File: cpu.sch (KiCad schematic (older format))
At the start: 26 parts, among them P27 BDM, U1 MC9S12XDP512, X1 16MHz

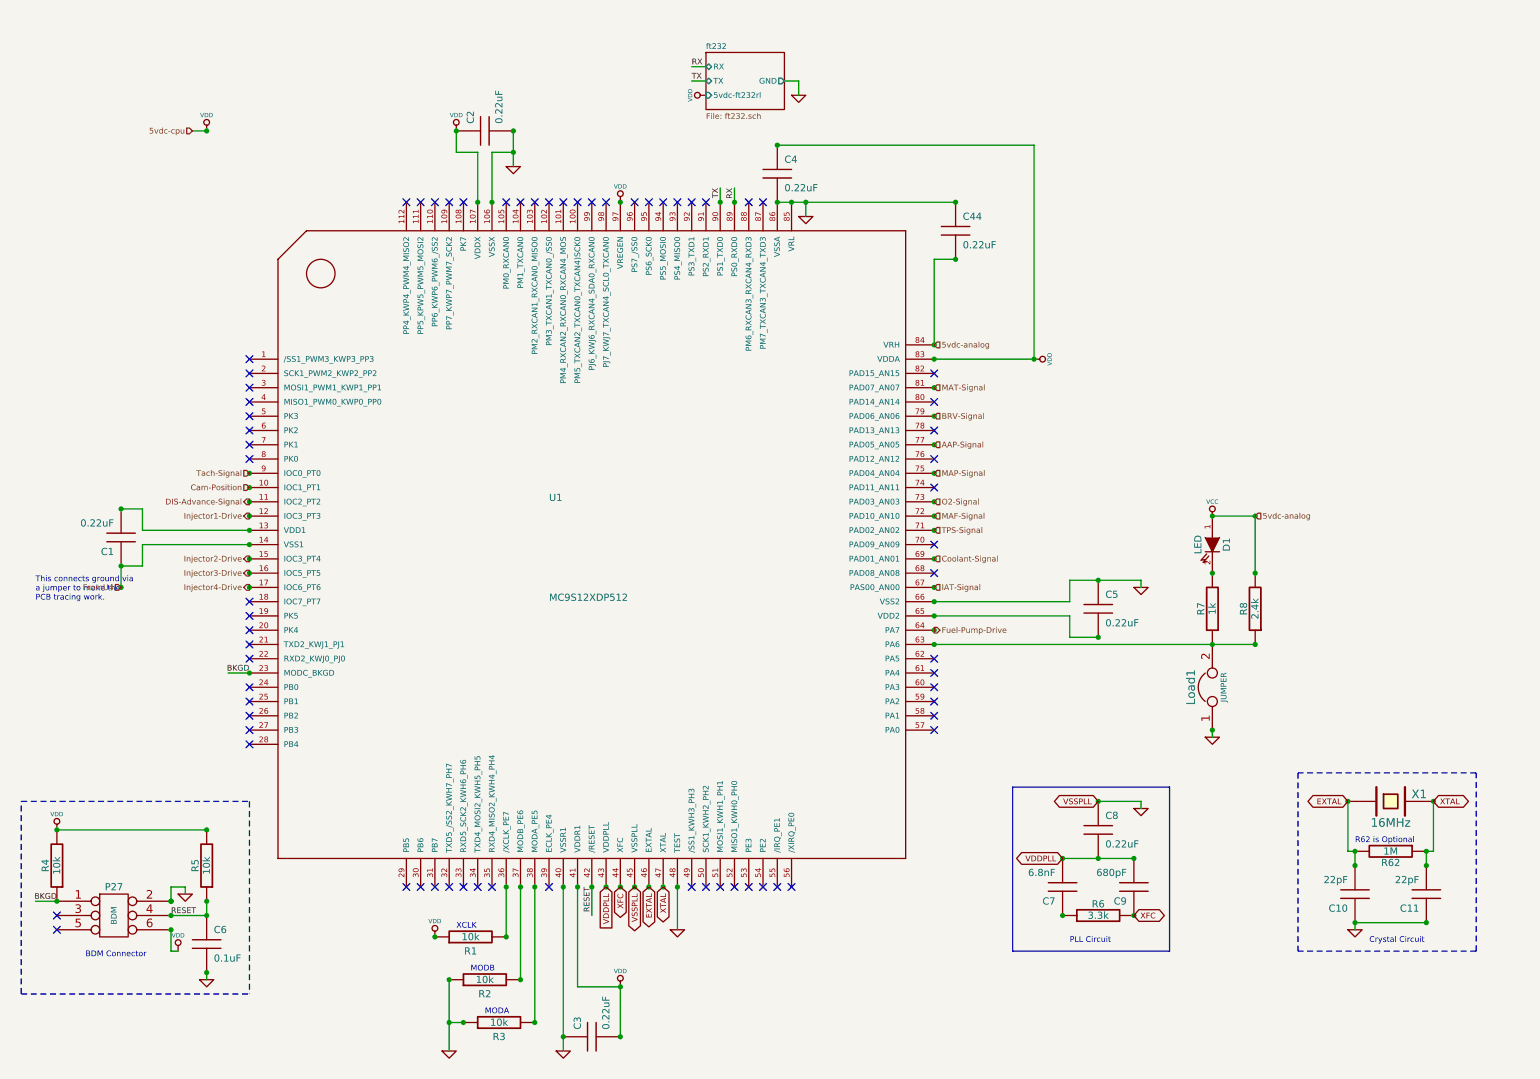
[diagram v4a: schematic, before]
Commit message: Fix MAX9926 Configuration and created new PCB and PDF
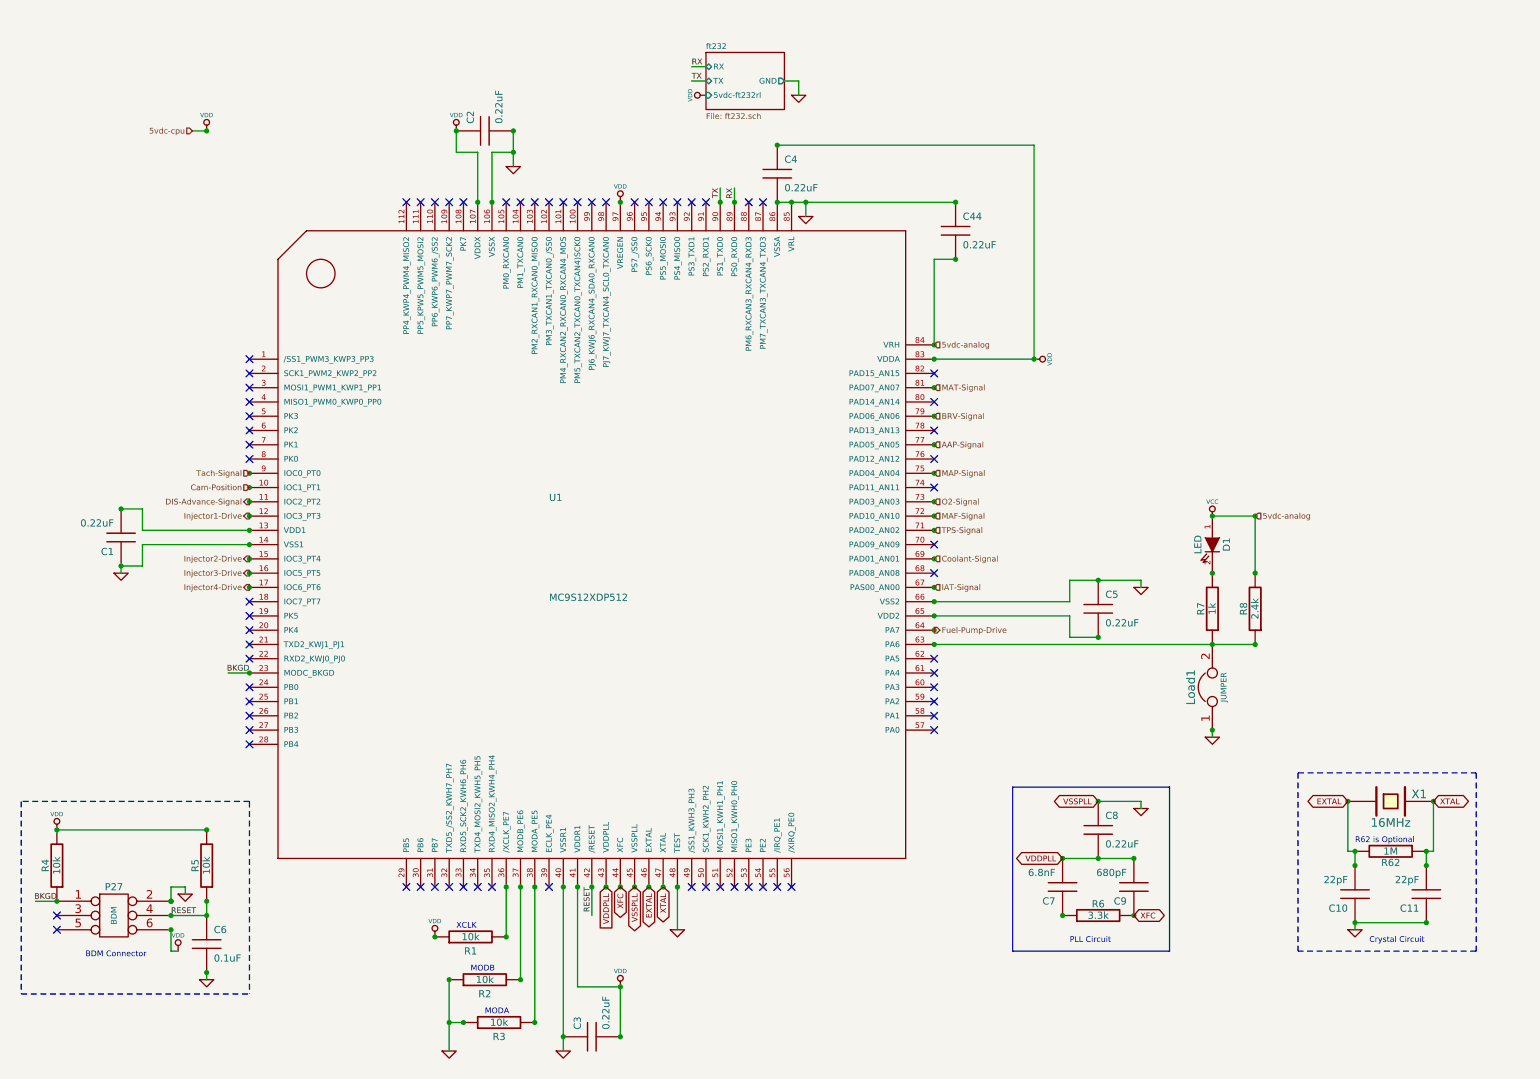
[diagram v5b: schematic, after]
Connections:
- net labels removed: FromU4
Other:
- note removed: "This connects ground via \na jumper to make the \nPCB tracing work."

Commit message: Updated Schematics and PDF, uploaded mc9s12xdp512 library
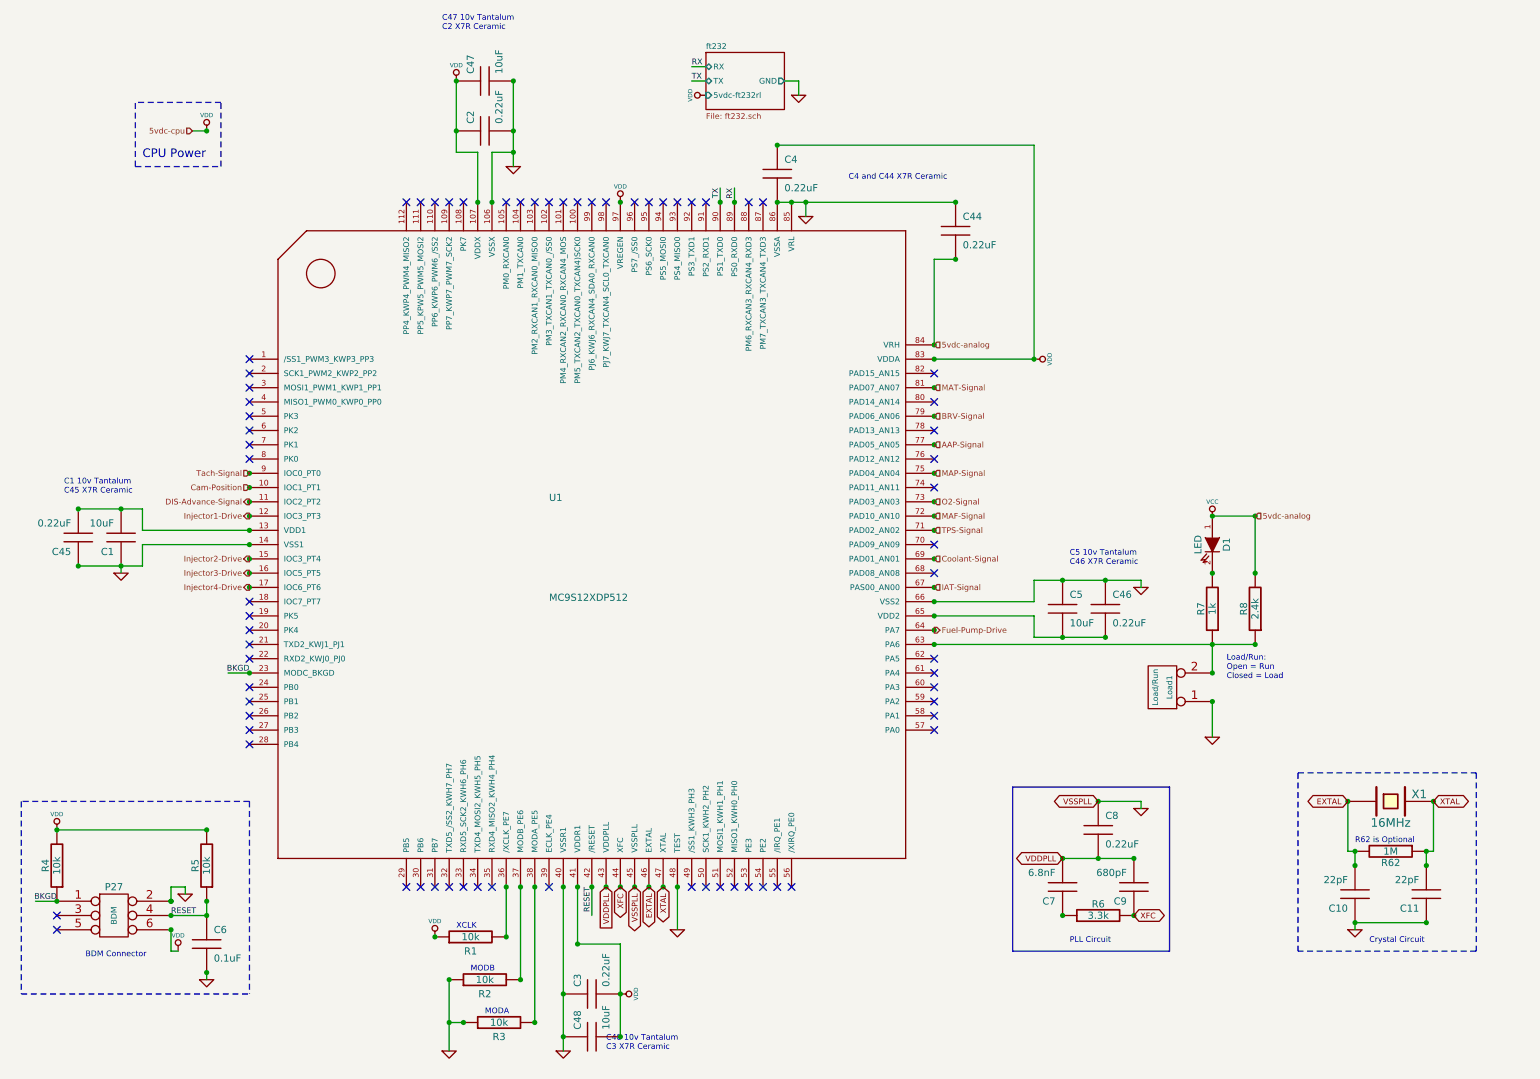
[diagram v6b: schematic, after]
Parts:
- removed Load1: JUMPER, symbol JUMPER
- added C45, C46: 0.22uF, symbol C
- added C47, C48: 10uF, symbol C
- added Load1: Load/Run, symbol CONN_2
- C1, C5: value 0.22uF -> 10uF
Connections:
- wire segments 71 -> 72
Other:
- note added: "C1 10v Tantalum\nC45 X7R Ceramic"
- note added: "C4 and C44 X7R Ceramic"
- note added: "C47 10v Tantalum\nC2 X7R Ceramic"
- note added: "C48 10v Tantalum\nC3 X7R Ceramic"
- note added: "C5 10v Tantalum\nC46 X7R Ceramic"
- note added: "CPU Power"
- note added: "Load/Run:\nOpen = Run\nClosed = Load"
- moved on the sheet: C3, C5
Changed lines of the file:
@@
-EESchema Schematic File Version 2  date Mon 23 Jan 2012 01:49:16 PM EST
+EESchema Schematic File Version 2  date Mon 23 Jan 2012 05:31:34 PM EST
 LIBS:power
 LIBS:device
@@
 EELAYER END
 $Descr A4 11700 8267
-Sheet 6 7
+Sheet 2 7
 Title "Jaguar PCB for FreeEMS"
 Date "23 jan 2012"
@@
 Comment4 ""
 $EndDescr
+Text Notes 6400 1600 0    40   ~ 0
+C4 and C44 X7R Ceramic
+Wire Notes Line
+	1400 1500 1400 1050
+Wire Wire Line
+	4800 7600 4800 6950
+Connection ~ 4500 6950
+Wire Wire Line
+	4800 6950 4500 6950
+Wire Wire Line
+	4050 1500 4050 900
+Wire Wire Line
+	7000 4550 7700 4550
+Wire Wire Line
+	7700 4550 7700 4400
+Wire Wire Line
+	7700 4400 8450 4400
+Wire Wire Line
+	1000 3900 1450 3900
 Wire Wire Line
 	1300 4350 1300 4300
-Wire Wire Line
-	1300 4300 1450 4300
 Connection ~ 6100 1750
 Wire Wire Line
-	5900 1750 7150 1750
+	7150 1750 5900 1750
 Connection ~ 7700 2850
 Wire Wire Line
@@
 Connection ~ 4050 1400
 Wire Wire Line
-	4050 1250 4050 1500
-Wire Wire Line
 	6100 1750 6100 1850
 Wire Wire Line
-	8450 4400 7950 4400
-Wire Wire Line
 	8450 4400 8450 4450
 Wire Wire Line
-	4400 6550 4400 7700
+	4400 7700 4400 6550
 Connection ~ 4100 7200
 Connection ~ 3600 7200
@@
 	4100 7200 4100 6550
 Wire Wire Line
-	3600 7200 3600 7700
-Wire Wire Line
-	4500 7250 4800 7250
-Wire Wire Line
-	4500 7250 4500 6550
+	3600 7700 3600 7200
+Wire Wire Line
+	4500 6950 4500 6550
 Connection ~ 7000 4850
 Connection ~ 7000 4750
@@
 Wire Wire Line
 	9250 3950 8950 3950
-Wire Wire Line
-	7950 4400 7950 4550
-Wire Wire Line
-	7950 4550 7000 4550
 Connection ~ 4050 1250
 Connection ~ 3650 1250
@@
 Connection ~ 1650 6650
 Wire Wire Line
-	7900 6350 8400 6350
+	8400 6350 7900 6350
 Wire Wire Line
 	10450 6300 10450 6400
@@
 	9950 6300 9950 6400
 Wire Wire Line
-	1300 3900 1450 3900
-Wire Wire Line
-	1450 3900 1450 4050
-Wire Wire Line
-	1450 4300 1450 4150
+	1450 4050 1450 3900
+Wire Wire Line
+	1450 4150 1450 4300
 Wire Wire Line
 	1450 4150 2200 4150
@@
 	3800 1400 3650 1400
 Wire Wire Line
-	3650 1400 3650 1250
-Wire Wire Line
 	700  6650 850  6650
 Wire Wire Line
-	7000 4650 7950 4650
-Wire Wire Line
-	7950 4650 7950 4800
-Wire Wire Line
-	7950 4800 8150 4800
-Connection ~ 8150 4400
-Connection ~ 8150 4800
-Wire Wire Line
-	9250 4850 7000 4850
+	7000 4850 9250 4850
 Connection ~ 8950 3950
 Connection ~ 9250 4350
@@
 Connection ~ 8950 4850
 Connection ~ 9250 4850
-Connection ~ 8950 5450
 Wire Wire Line
 	4600 6550 4600 6750
 Connection ~ 4600 6550
-Wire Wire Line
-	4800 7250 4800 7600
 Connection ~ 4800 7600
 Connection ~ 4400 7600
@@
 	9950 6800 9950 6850
 Wire Wire Line
-	8950 5500 8950 5450
-Wire Wire Line
 	1650 6650 1650 6550
 Wire Wire Line
@@
 Wire Wire Line
 	5200 6550 5200 6850
-Connection ~ 4800 7250
 Wire Wire Line
 	1700 7000 1650 7000
@@
 Connection ~ 9250 3950
 Connection ~ 1300 4300
+Wire Wire Line
+	8950 4850 8950 5050
+Wire Wire Line
+	8950 5500 8950 5250
+Connection ~ 8950 5050
+Connection ~ 8950 5250
+Wire Wire Line
+	1450 4300 1000 4300
+Connection ~ 1000 3900
+Connection ~ 1000 4300
+Wire Wire Line
+	7000 4650 7700 4650
+Wire Wire Line
+	7700 4650 7700 4800
+Wire Wire Line
+	7700 4800 8200 4800
+Connection ~ 8200 4400
+Connection ~ 8200 4800
+Connection ~ 7900 4800
+Connection ~ 7900 4400
+Wire Wire Line
+	3650 1400 3650 900
+Connection ~ 3650 900
+Connection ~ 4050 900
+Connection ~ 4400 7300
+Connection ~ 4800 7300
+Wire Notes Line
+	1400 1500 2000 1500
+Wire Notes Line
+	2000 1500 2000 1050
+Wire Notes Line
+	2000 1050 1400 1050
+Text Notes 1450 1450 0    60   ~ 0
+CPU Power
+Text Notes 4700 7700 0    40   ~ 0
+C48 10v Tantalum\nC3 X7R Ceramic
+Text Notes 3550 550  0    40   ~ 0
+C47 10v Tantalum\nC2 X7R Ceramic
+$Comp
+L C C48
+U 1 1 4F1DD593
+P 4600 7600
+F 0 "C48" H 4650 7700 50  0000 L CNN
+F 1 "10uF" H 4650 7500 50  0000 L CNN
+	1    4600 7600
+	0    -1   -1   0
+$EndComp
+$Comp
+L C C47
+U 1 1 4F1DD576
+P 3850 900
+F 0 "C47" H 3900 1000 50  0000 L CNN
+F 1 "10uF" H 3900 800 50  0000 L CNN
+	1    3850 900
+	0    -1   -1   0
+$EndComp
+$Comp
+L C C46
+U 1 1 4F1DD206
+P 8200 4600
+F 0 "C46" H 8250 4700 50  0000 L CNN
+F 1 "0.22uF" H 8250 4500 50  0000 L CNN
+	1    8200 4600
+	1    0    0    -1
+$EndComp
+$Comp
+L C C45
+U 1 1 4F1DD1E9
+P 1000 4100
+F 0 "C45" H 1050 4200 50  0000 L CNN
+F 1 "0.22uF" H 1050 4000 50  0000 L CNN
+	1    1000 4100
+	-1   0    0    1
+$EndComp
+Text Notes 9050 5100 0    40   ~ 0
+Load/Run:\nOpen = Run\nClosed = Load
+Text Notes 900  3800 0    40   ~ 0
+C1 10v Tantalum\nC45 X7R Ceramic
+Text Notes 7950 4300 0    40   ~ 0
+C5 10v Tantalum\nC46 X7R Ceramic
+$Comp
+L CONN_2 Load1
+U 1 1 4F1DBE71
+P 8600 5150
+F 0 "Load1" V 8550 5150 40  0000 C CNN
+F 1 "Load/Run" V 8650 5150 40  0000 C CNN
+	1    8600 5150
+	-1   0    0    1
+$EndComp
 $Comp
 L GND #PWR02
@@
 L VDD #PWR08
 U 1 1 4F1C3179
-P 4800 7250
-F 0 "#PWR08" H 4800 7350 30  0001 C CNN
-F 1 "VDD" H 4800 7360 30  0000 C CNN
-	1    4800 7250
-	1    0    0    -1
+P 4800 7300
+F 0 "#PWR08" H 4800 7400 30  0001 C CNN
+F 1 "VDD" H 4800 7410 30  0000 C CNN
+	1    4800 7300
+	0    1    1    0
 $EndComp
 $Comp
@@
 L VDD #PWR014
 U 1 1 4F1C30DD
-P 3650 1250
-F 0 "#PWR014" H 3650 1350 30  0001 C CNN
-F 1 "VDD" H 3650 1360 30  0000 C CNN
-	1    3650 1250
+P 3650 900
+F 0 "#PWR014" H 3650 1000 30  0001 C CNN
+F 1 "VDD" H 3650 1010 30  0000 C CNN
+	1    3650 900
 	1    0    0    -1
 $EndComp
@@
 Text HLabel 7000 2750 2    40   Input ~ 0
 5vdc-analog
-$Comp
-L JUMPER Load1
-U 1 1 4F1B0199
-P 8950 5150
-F 0 "Load1" H 8950 5300 60  0000 C CNN
-F 1 "JUMPER" H 8950 5070 40  0000 C CNN
-	1    8950 5150
-	0    -1   -1   0
-$EndComp
 Text HLabel 1800 1250 0    40   Input ~ 0
 5vdc-cpu
@@
 L C C3
 U 1 1 4F0A3455
-P 4600 7600
-F 0 "C3" H 4650 7700 50  0000 L CNN
-F 1 "0.22uF" H 4650 7500 50  0000 L CNN
-	1    4600 7600
+P 4600 7300
+F 0 "C3" H 4650 7400 50  0000 L CNN
+F 1 "0.22uF" H 4650 7200 50  0000 L CNN
+	1    4600 7300
 	0    -1   -1   0
 $EndComp
@@
 P 1300 4100
 F 0 "C1" H 1350 4200 50  0000 L CNN
-F 1 "0.22uF" H 1350 4000 50  0000 L CNN
+F 1 "10uF" H 1350 4000 50  0000 L CNN
 	1    1300 4100
 	-1   0    0    1
@@
 L C C5
 U 1 1 4F0A3335
-P 8150 4600
-F 0 "C5" H 8200 4700 50  0000 L CNN
-F 1 "0.22uF" H 8200 4500 50  0000 L CNN
-	1    8150 4600
-	1    0    0    -1
-$EndComp
+P 7900 4600
+F 0 "C5" H 7950 4700 50  0000 L CNN
+F 1 "10uF" H 7950 4500 50  0000 L CNN
+	1    7900 4600
+	1    0    0    -1
+$EndComp

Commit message: Changed CPU Power caps, updated Jaguar.ods (BOM) and PDF
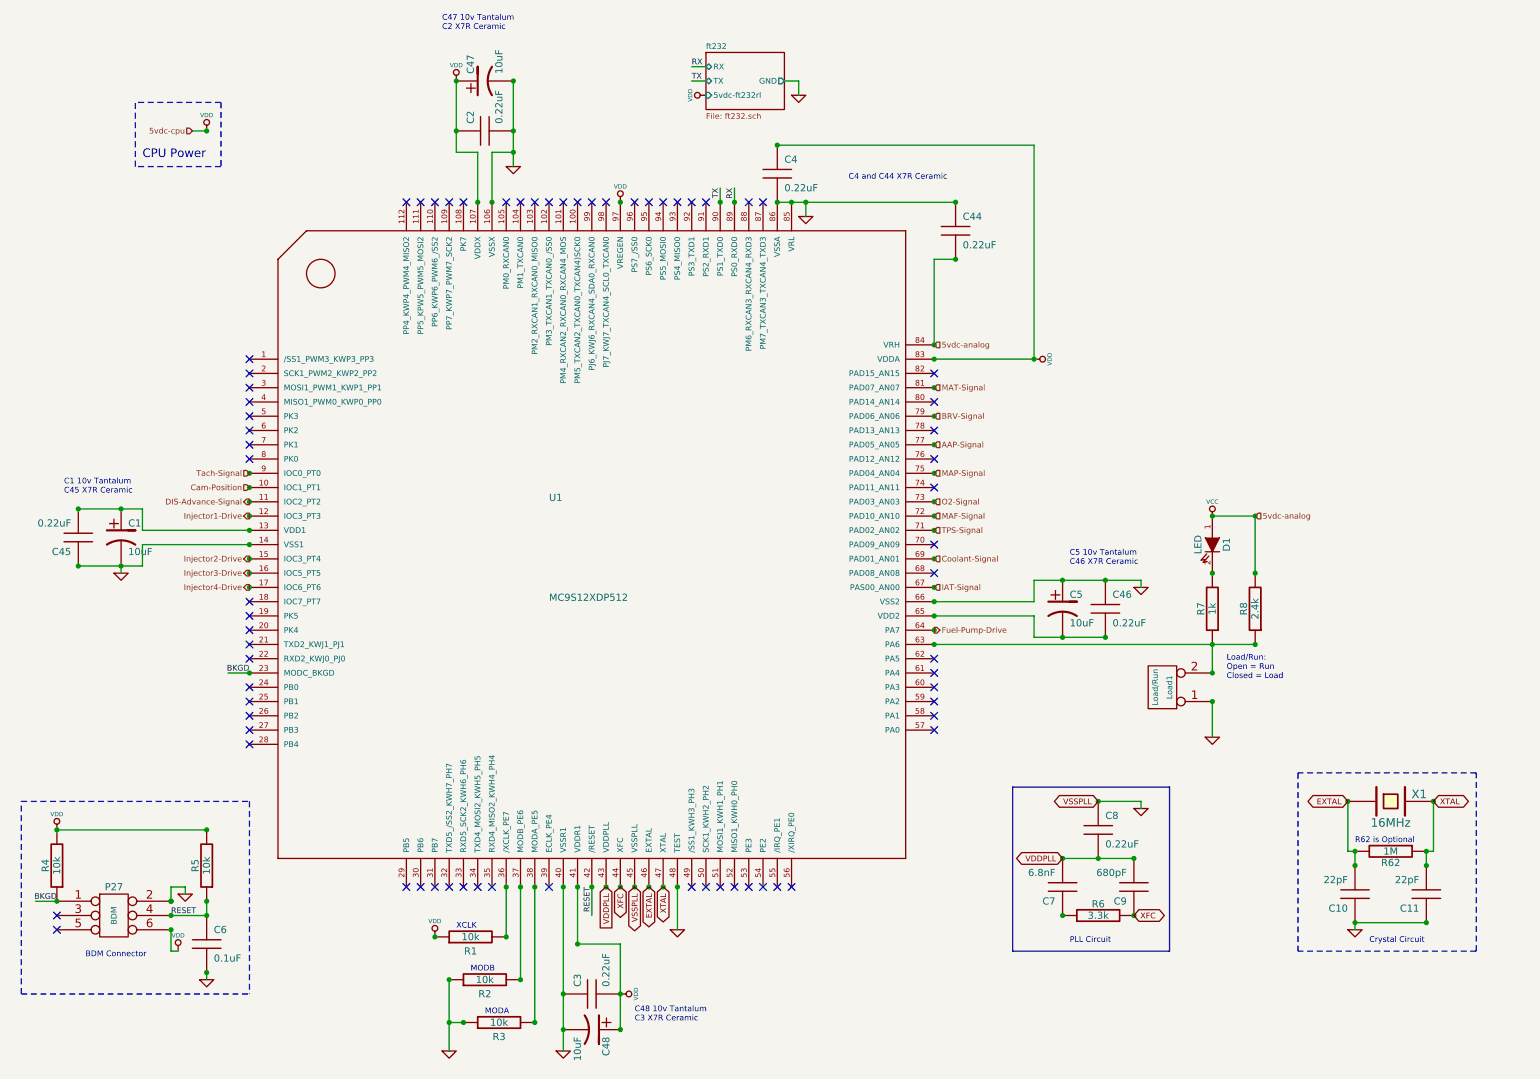
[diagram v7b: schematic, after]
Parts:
- removed C1, C47, C48, C5: 10uF, symbol C
- added C1, C47, C48, C5: 10uF, symbol CP1
